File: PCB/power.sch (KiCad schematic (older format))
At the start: 47 parts, among them J801 V_IN, Q801 AOD4189, U801 ACS712xLCTR-20A, U802 NCP1117-5.0_SOT223, U803 L5973D, U804 NCP1117-3.3_SOT223

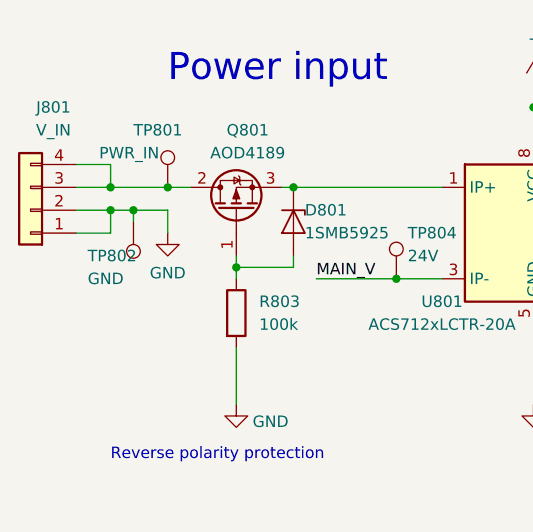
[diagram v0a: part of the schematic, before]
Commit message: PCB: create new layout for power supply, route LED signalization and reset
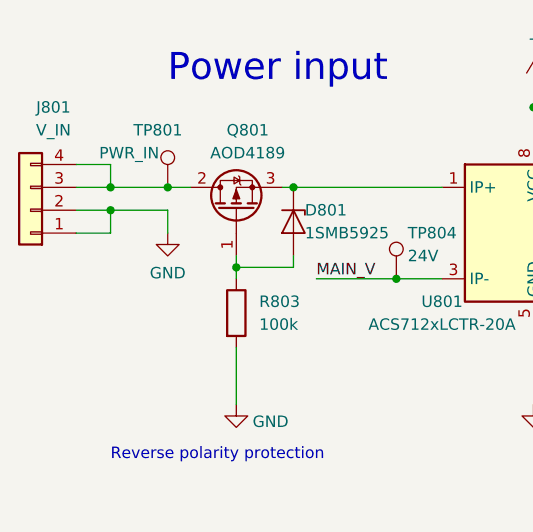
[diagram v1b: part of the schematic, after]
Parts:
- removed TP802: GND, TestPoint:TestPoint_THTPad_D1.0mm_Drill0.5mm, symbol Connector:TestPoint
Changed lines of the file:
@@
 $EndComp
-Wire Wire Line
-	1450 1400 1550 1400
 Wire Wire Line
 	1700 1400 1700 1500
-$Comp
-L Connector:TestPoint TP802
-U 1 1 5CDB03CA
-P 1550 1450
-F 0 "TP802" H 1750 1600 50  0000 R CNN
-F 1 "GND" H 1750 1700 50  0000 R CNN
-F 2 "TestPoint:TestPoint_THTPad_D1.0mm_Drill0.5mm" H 1750 1450 50  0001 C CNN
-F 3 "~" H 1750 1450 50  0001 C CNN
-	1    1550 1450
-	-1   0    0    1
-$EndComp
-Wire Wire Line
-	1550 1400 1700 1400
-Connection ~ 1550 1400
 $Comp
 L Device:Q_PMOS_GDS Q801
@@
 	1    0    0    -1
 $EndComp
-Wire Wire Line
-	1550 1450 1550 1400
 $Comp
 L Regulator_Switching:L5973D U803
@@
 	6825 975  6825 1100
 Connection ~ 6825 975
+Wire Wire Line
+	1450 1400 1700 1400
 $EndSCHEMATC
